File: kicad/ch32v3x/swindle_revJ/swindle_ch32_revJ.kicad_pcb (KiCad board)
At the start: 2 copper layers, 49.8 x 33.3 mm, 65 parts, among them J1 jtag, J10 Debug port, J2 Conn_01x03_Socket, J2_DFU1 con2, J3 Dbg, J4 USB, J5 Debug port, J6 Debug port, J7 Conn_01x03_Pin, J8 Debug port, J9 Conn_01x03_Pin, U1 CH32V303RCT6, U2 LM1117-3.3, U3 3V->VTREF, U4 VTREF->3V, U5 VTREF<->3V, U6 RT9013-33GB, Y1 8Mhz

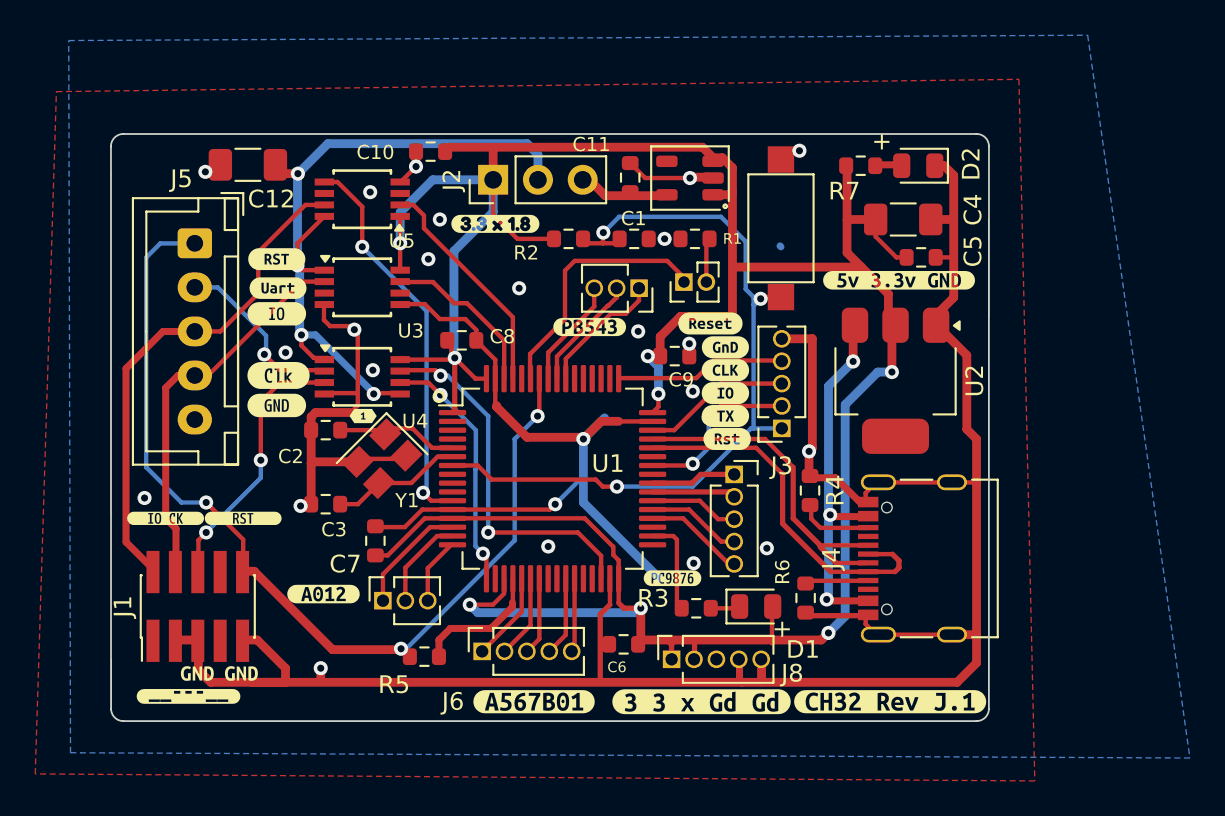
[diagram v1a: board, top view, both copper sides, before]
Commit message: Kicad update: ch32: update pcb , add boot pin control ch32: Ground PB2 so that the internal bootloader is on USB rp_zero_mini :add mostfet to rp zero mini
general update
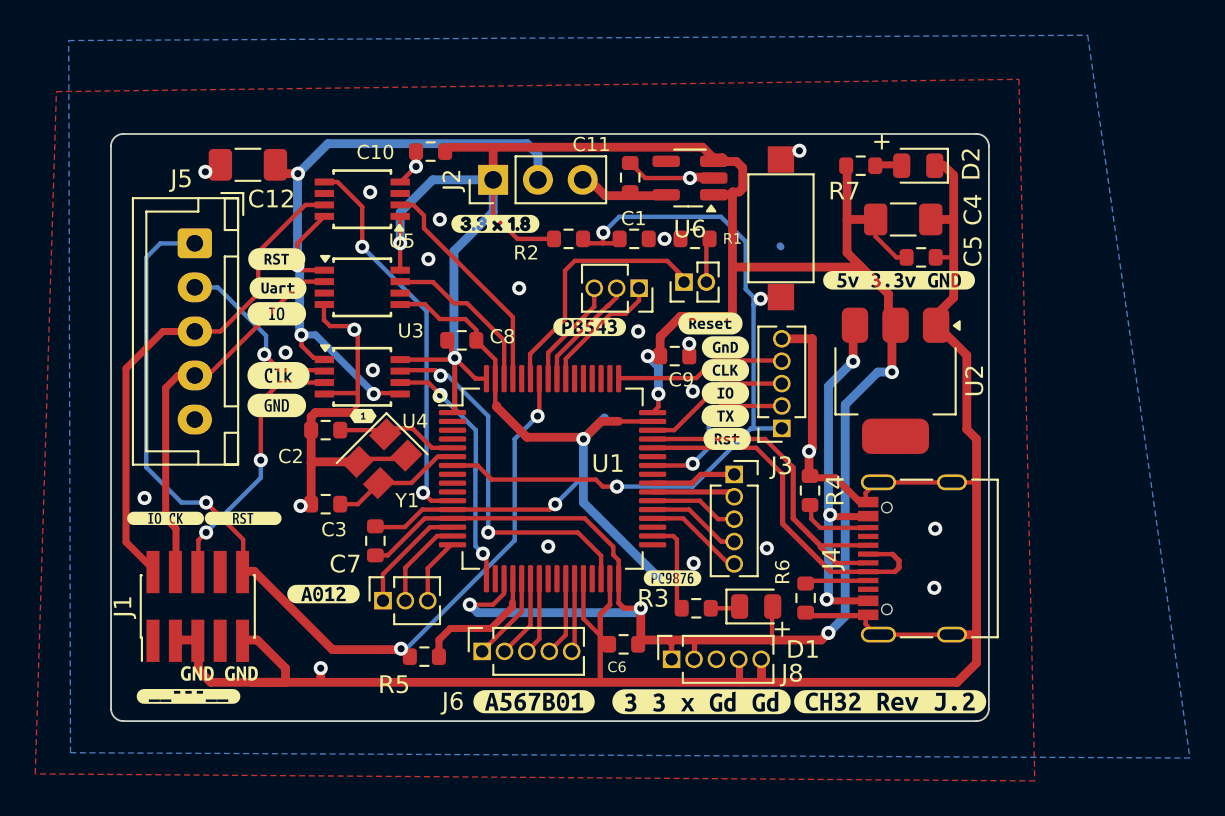
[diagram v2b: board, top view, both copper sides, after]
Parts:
- removed kibuzzard-6869421E: G***, kibuzzard-6869421E
- added kibuzzard-6A65D8DC: G***, kibuzzard-6A65D8DC, F.Cu at (149.7, 99.1)
- U6: footprint PCM_Package_TO_SOT_SMD_AKL:TSOT-23-5 -> Package_TO_SOT_SMD:SOT-23-5_HandSoldering
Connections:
- U1 pad 28: unconnected-(U1-PB2-Pad28) -> GND
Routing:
- net GND: track 200.5 -> 204.8 mm, vias 24 -> 26
- net +3.3V: track 163.6 -> 164.7 mm
